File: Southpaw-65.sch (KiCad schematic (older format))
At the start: 205 parts, among them J1 USB_C_Receptacle_USB2.0, SW1 SW_Push, U1 ATmega32A-PU, Y1 16MHz

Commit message: More wiring
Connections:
- net COL0: now also U1.4 (PB3); no longer U1.35 (PA5)
- net COL1: now also U1.3 (PB2); no longer U1.34 (PA6)
- net COL10: no longer U1.8 (PB7)
- net COL11: no longer U1.22 (PC0)
- net COL12: no longer U1.23 (PC1)
- net COL13: no longer U1.24 (PC2)
- net COL14: no longer U1.25 (PC3)
- net COL15: no longer U1.26 (PC4)
- net COL16: no longer U1.27 (PC5)
- net COL17: no longer U1.28 (PC6)
- net COL18: no longer U1.29 (PC7)
- net COL19: no longer U1.14 (PD0)
- net COL2: now also U1.2 (PB1); no longer U1.33 (PA7)
- net COL4: now also U1.39 (PA1); no longer U1.2 (PB1)
- net COL5: now also U1.40 (PA0); no longer U1.3 (PB2)
- net COL6: no longer U1.4 (PB3)
- net COL7: no longer U1.5 (PB4)
- net COL8: no longer U1.6 (PB5)
- net COL9: no longer U1.7 (PB6)
- net ROW0: now also U1.5 (PB4); no longer U1.40 (PA0)
- net ROW1: now also U1.6 (PB5); no longer U1.39 (PA1)
- net ROW2: now also U1.7 (PB6); no longer U1.38 (PA2)
- net ROW3: now also U1.8 (PB7); no longer U1.37 (PA3)
- net ROW4: now also U1.14 (PD0); no longer U1.36 (PA4)
- no-connect marks 3 -> 0
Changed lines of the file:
@@
 Wire Wire Line
 	17400 3350 17400 4000
-Text GLabel 2000 1050 2    50   Input ~ 0
+Text GLabel 2000 2350 2    50   Input ~ 0
 ROW0
-Text GLabel 2000 1150 2    50   Input ~ 0
+Text GLabel 2000 2450 2    50   Input ~ 0
 ROW1
-Text GLabel 2000 1250 2    50   Input ~ 0
+Text GLabel 2000 2550 2    50   Input ~ 0
 ROW2
-Text GLabel 2000 1350 2    50   Input ~ 0
+Text GLabel 2000 2650 2    50   Input ~ 0
 ROW3
-Text GLabel 2000 1450 2    50   Input ~ 0
-ROW4
-Text GLabel 2000 1550 2    50   Input ~ 0
+Text GLabel 2000 2250 2    50   Input ~ 0
 COL0
-Text GLabel 2000 1650 2    50   Input ~ 0
+Text GLabel 2000 2150 2    50   Input ~ 0
 COL1
-Text GLabel 2000 1750 2    50   Input ~ 0
+Text GLabel 2000 2050 2    50   Input ~ 0
 COL2
 Text GLabel 2000 1950 2    50   Input ~ 0
 COL3
-Text GLabel 2000 2050 2    50   Input ~ 0
+Text GLabel 2000 1150 2    50   Input ~ 0
 COL4
-Text GLabel 2000 2150 2    50   Input ~ 0
+Text GLabel 2000 1050 2    50   Input ~ 0
 COL5
-Text GLabel 2000 2250 2    50   Input ~ 0
+Text GLabel 3050 2250 2    50   Input ~ 0
 COL6
-Text GLabel 2000 2350 2    50   Input ~ 0
+Text GLabel 3050 2350 2    50   Input ~ 0
 COL7
-Text GLabel 2000 2450 2    50   Input ~ 0
+Text GLabel 3050 2450 2    50   Input ~ 0
 COL8
-Text GLabel 2000 2550 2    50   Input ~ 0
+Text GLabel 3050 2550 2    50   Input ~ 0
 COL9
-Text GLabel 2000 2650 2    50   Input ~ 0
+Text GLabel 3050 2650 2    50   Input ~ 0
 COL10
-Text GLabel 2000 2850 2    50   Input ~ 0
+Text GLabel 3050 2850 2    50   Input ~ 0
 COL11
-Text GLabel 2000 2950 2    50   Input ~ 0
+Text GLabel 3050 2950 2    50   Input ~ 0
 COL12
-Text GLabel 2000 3050 2    50   Input ~ 0
+Text GLabel 3050 3050 2    50   Input ~ 0
 COL13
-Text GLabel 2000 3150 2    50   Input ~ 0
+Text GLabel 3050 3150 2    50   Input ~ 0
 COL14
-Text GLabel 2000 3250 2    50   Input ~ 0
+Text GLabel 3050 3250 2    50   Input ~ 0
 COL15
-Text GLabel 2000 3350 2    50   Input ~ 0
+Text GLabel 3050 3350 2    50   Input ~ 0
 COL16
-Text GLabel 2000 3450 2    50   Input ~ 0
+Text GLabel 3050 3450 2    50   Input ~ 0
 COL17
-Text GLabel 2000 3550 2    50   Input ~ 0
+Text GLabel 3050 3550 2    50   Input ~ 0
 COL18
-Text GLabel 2000 3750 2    50   Input ~ 0
+Text GLabel 3050 3750 2    50   Input ~ 0
 COL19
 $Comp
@@
 Wire Wire Line
 	1400 750  1400 700
-Connection ~ 1400 750
 $Comp
 L power:GND #PWR0110
@@
 Wire Wire Line
 	2800 4050 2700 4050
-$Comp
-L MCU_Microchip_ATmega:ATmega32A-PU U1
-U 1 1 5F901AE8
-P 1400 2750
-F 0 "U1" H 1400 661 50  0000 C CNN
-F 1 "ATmega32A-PU" H 1400 570 50  0000 C CNN
-F 2 "Package_DIP:DIP-40_W15.24mm" H 1400 2750 50  0001 C CIN
-F 3 "http://ww1.microchip.com/downloads/en/DeviceDoc/atmel-8155-8-bit-microcontroller-avr-atmega32a_datasheet.pdf" H 1400 2750 50  0001 C CNN
-	1    1400 2750
-	1    0    0    -1
-$EndComp
-NoConn ~ 2000 4450
-NoConn ~ 2000 4350
-NoConn ~ 2000 3850
 Wire Wire Line
 	14950 2050 14950 2700
@@
 Wire Wire Line
 	16200 1250 16200 1400
+Text GLabel 2000 3750 2    50   Input ~ 0
+ROW4
+Connection ~ 1400 750
+$Comp
+L MCU_Microchip_ATmega:ATmega32A-PU U1
+U 1 1 5F901AE8
+P 1400 2750
+F 0 "U1" H 1400 661 50  0000 C CNN
+F 1 "ATmega32A-PU" H 1400 570 50  0000 C CNN
+F 2 "Package_DIP:DIP-40_W15.24mm" H 1400 2750 50  0001 C CIN
+F 3 "http://ww1.microchip.com/downloads/en/DeviceDoc/atmel-8155-8-bit-microcontroller-avr-atmega32a_datasheet.pdf" H 1400 2750 50  0001 C CNN
+	1    1400 2750
+	1    0    0    -1
+$EndComp
 $EndSCHEMATC

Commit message: Lots of wiring to MCU done
Considering redoing it because thicc bottom
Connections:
- net COL10: now also U1.34 (PA6)
- net COL11: now also U1.35 (PA5)
- net COL12: now also U1.36 (PA4)
- net COL13: now also U1.37 (PA3)
- net COL14: now also U1.38 (PA2)
- net COL15: now also U1.24 (PC2)
- net COL16: now also U1.25 (PC3)
- net COL17: now also U1.27 (PC5)
- net COL18: now also U1.15 (PD1)
- net COL19: now also U1.20 (PD6)
- net COL7: now also U1.29 (PC7)
- net COL8: now also U1.32 (AREF)
- net COL9: now also U1.33 (PA7)
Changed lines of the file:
@@
 Text GLabel 2000 1050 2    50   Input ~ 0
 COL5
-Text GLabel 3050 2250 2    50   Input ~ 0
-COL6
-Text GLabel 3050 2350 2    50   Input ~ 0
-COL7
-Text GLabel 3050 2450 2    50   Input ~ 0
+Text GLabel 800  1650 0    50   Input ~ 0
 COL8
-Text GLabel 3050 2550 2    50   Input ~ 0
+Text GLabel 2000 1750 2    50   Input ~ 0
 COL9
-Text GLabel 3050 2650 2    50   Input ~ 0
+Text GLabel 2000 1650 2    50   Input ~ 0
 COL10
-Text GLabel 3050 2850 2    50   Input ~ 0
+Text GLabel 2000 1550 2    50   Input ~ 0
 COL11
-Text GLabel 3050 2950 2    50   Input ~ 0
+Text GLabel 2000 1450 2    50   Input ~ 0
 COL12
-Text GLabel 3050 3050 2    50   Input ~ 0
+Text GLabel 2000 1350 2    50   Input ~ 0
 COL13
-Text GLabel 3050 3150 2    50   Input ~ 0
+Text GLabel 2000 1250 2    50   Input ~ 0
 COL14
-Text GLabel 3050 3250 2    50   Input ~ 0
+Text GLabel 2000 3050 2    50   Input ~ 0
 COL15
-Text GLabel 3050 3350 2    50   Input ~ 0
+Text GLabel 2000 3150 2    50   Input ~ 0
 COL16
-Text GLabel 3050 3450 2    50   Input ~ 0
+Text GLabel 2000 3350 2    50   Input ~ 0
 COL17
-Text GLabel 3050 3550 2    50   Input ~ 0
+Text GLabel 2000 3850 2    50   Input ~ 0
 COL18
-Text GLabel 3050 3750 2    50   Input ~ 0
+Text GLabel 2000 4350 2    50   Input ~ 0
 COL19
 $Comp
@@
 	1    0    0    -1
 $EndComp
+Text GLabel 2000 3550 2    50   Input ~ 0
+COL7
+Text GLabel 3050 2250 2    50   Input ~ 0
+COL6
 $EndSCHEMATC

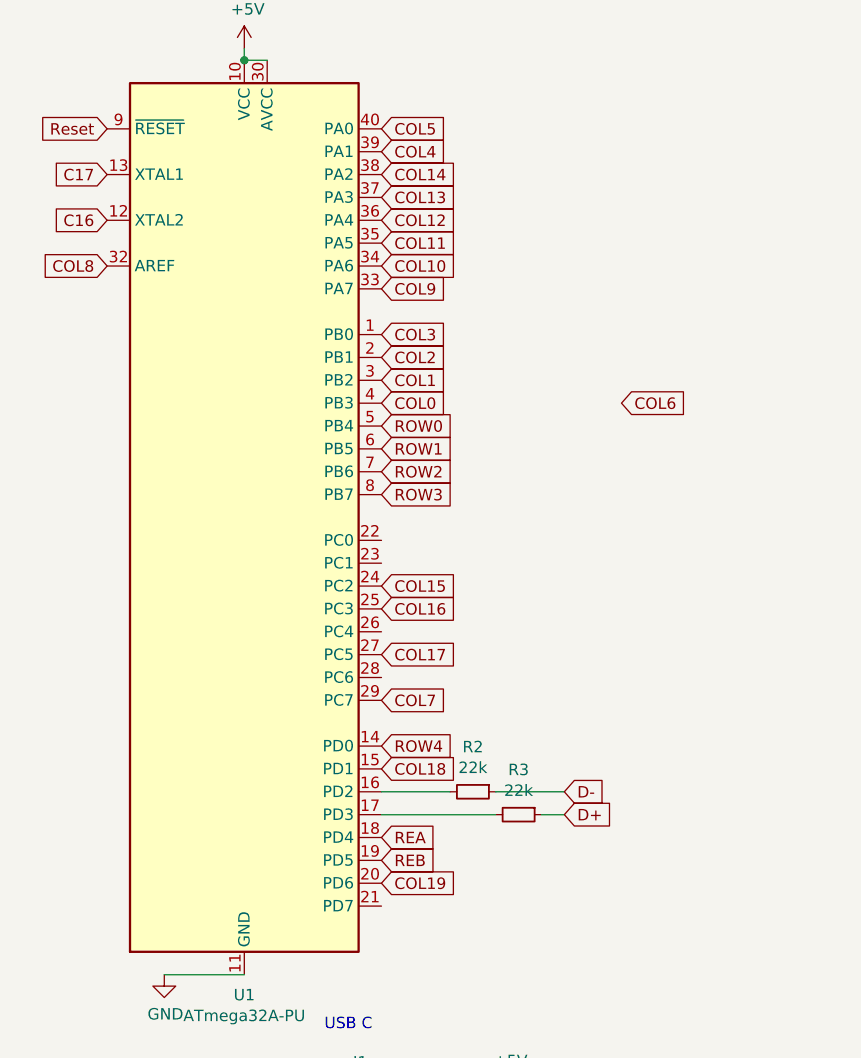
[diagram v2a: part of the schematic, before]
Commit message: Redid wirings
Decrease in space between pcb bottom, and switches
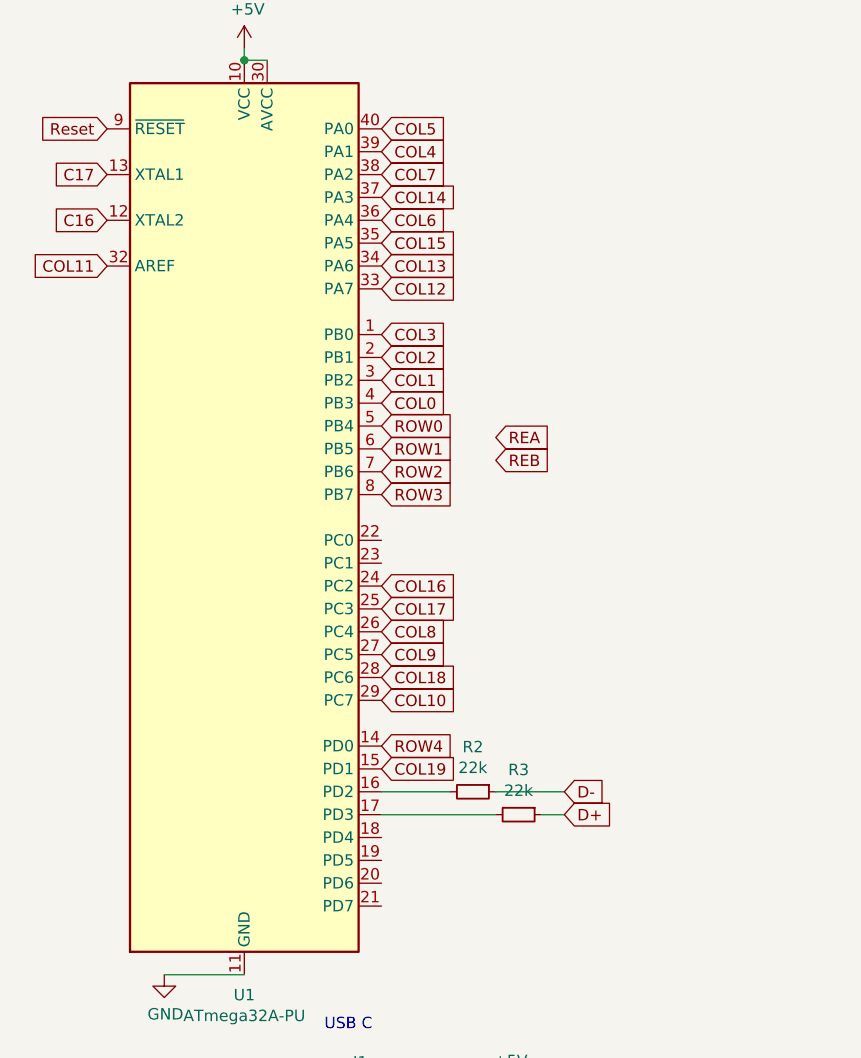
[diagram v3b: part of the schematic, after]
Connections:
- net COL10: now also U1.29 (PC7); no longer U1.34 (PA6)
- net COL11: now also U1.32 (AREF); no longer U1.35 (PA5)
- net COL12: now also U1.33 (PA7); no longer U1.36 (PA4)
- net COL13: now also U1.34 (PA6); no longer U1.37 (PA3)
- net COL14: now also U1.37 (PA3); no longer U1.38 (PA2)
- net COL15: now also U1.35 (PA5); no longer U1.24 (PC2)
- net COL16: now also U1.24 (PC2); no longer U1.25 (PC3)
- net COL17: now also U1.25 (PC3); no longer U1.27 (PC5)
- net COL18: now also U1.28 (PC6); no longer U1.15 (PD1)
- net COL19: now also U1.15 (PD1); no longer U1.20 (PD6)
- net COL6: now also U1.36 (PA4)
- net COL7: now also U1.38 (PA2); no longer U1.29 (PC7)
- net COL8: now also U1.26 (PC4); no longer U1.32 (AREF)
- net COL9: now also U1.27 (PC5); no longer U1.33 (PA7)
- net REA: no longer U1.18 (PD4)
- net REB: no longer U1.19 (PD5)
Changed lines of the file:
@@
 Text GLabel 2000 1050 2    50   Input ~ 0
 COL5
+Text GLabel 2000 3250 2    50   Input ~ 0
+COL8
+Text GLabel 2000 3350 2    50   Input ~ 0
+COL9
+Text GLabel 2000 3550 2    50   Input ~ 0
+COL10
 Text GLabel 800  1650 0    50   Input ~ 0
-COL8
+COL11
 Text GLabel 2000 1750 2    50   Input ~ 0
-COL9
+COL12
 Text GLabel 2000 1650 2    50   Input ~ 0
-COL10
+COL13
+Text GLabel 2000 1350 2    50   Input ~ 0
+COL14
 Text GLabel 2000 1550 2    50   Input ~ 0
-COL11
-Text GLabel 2000 1450 2    50   Input ~ 0
-COL12
-Text GLabel 2000 1350 2    50   Input ~ 0
-COL13
-Text GLabel 2000 1250 2    50   Input ~ 0
-COL14
+COL15
 Text GLabel 2000 3050 2    50   Input ~ 0
-COL15
+COL16
 Text GLabel 2000 3150 2    50   Input ~ 0
-COL16
-Text GLabel 2000 3350 2    50   Input ~ 0
 COL17
+Text GLabel 2000 3450 2    50   Input ~ 0
+COL18
 Text GLabel 2000 3850 2    50   Input ~ 0
-COL18
-Text GLabel 2000 4350 2    50   Input ~ 0
 COL19
 $Comp
@@
 Text Notes 5250 5000 0    50   ~ 0
 Reset
-Text GLabel 2000 4150 2    50   Input ~ 0
+Text GLabel 2500 2400 2    50   Input ~ 0
 REA
-Text GLabel 2000 4250 2    50   Input ~ 0
+Text GLabel 2500 2500 2    50   Input ~ 0
 REB
 Wire Wire Line
@@
 	1    0    0    -1
 $EndComp
-Text GLabel 2000 3550 2    50   Input ~ 0
+Text GLabel 2000 1250 2    50   Input ~ 0
 COL7
-Text GLabel 3050 2250 2    50   Input ~ 0
+Text GLabel 2000 1450 2    50   Input ~ 0
 COL6
 $EndSCHEMATC

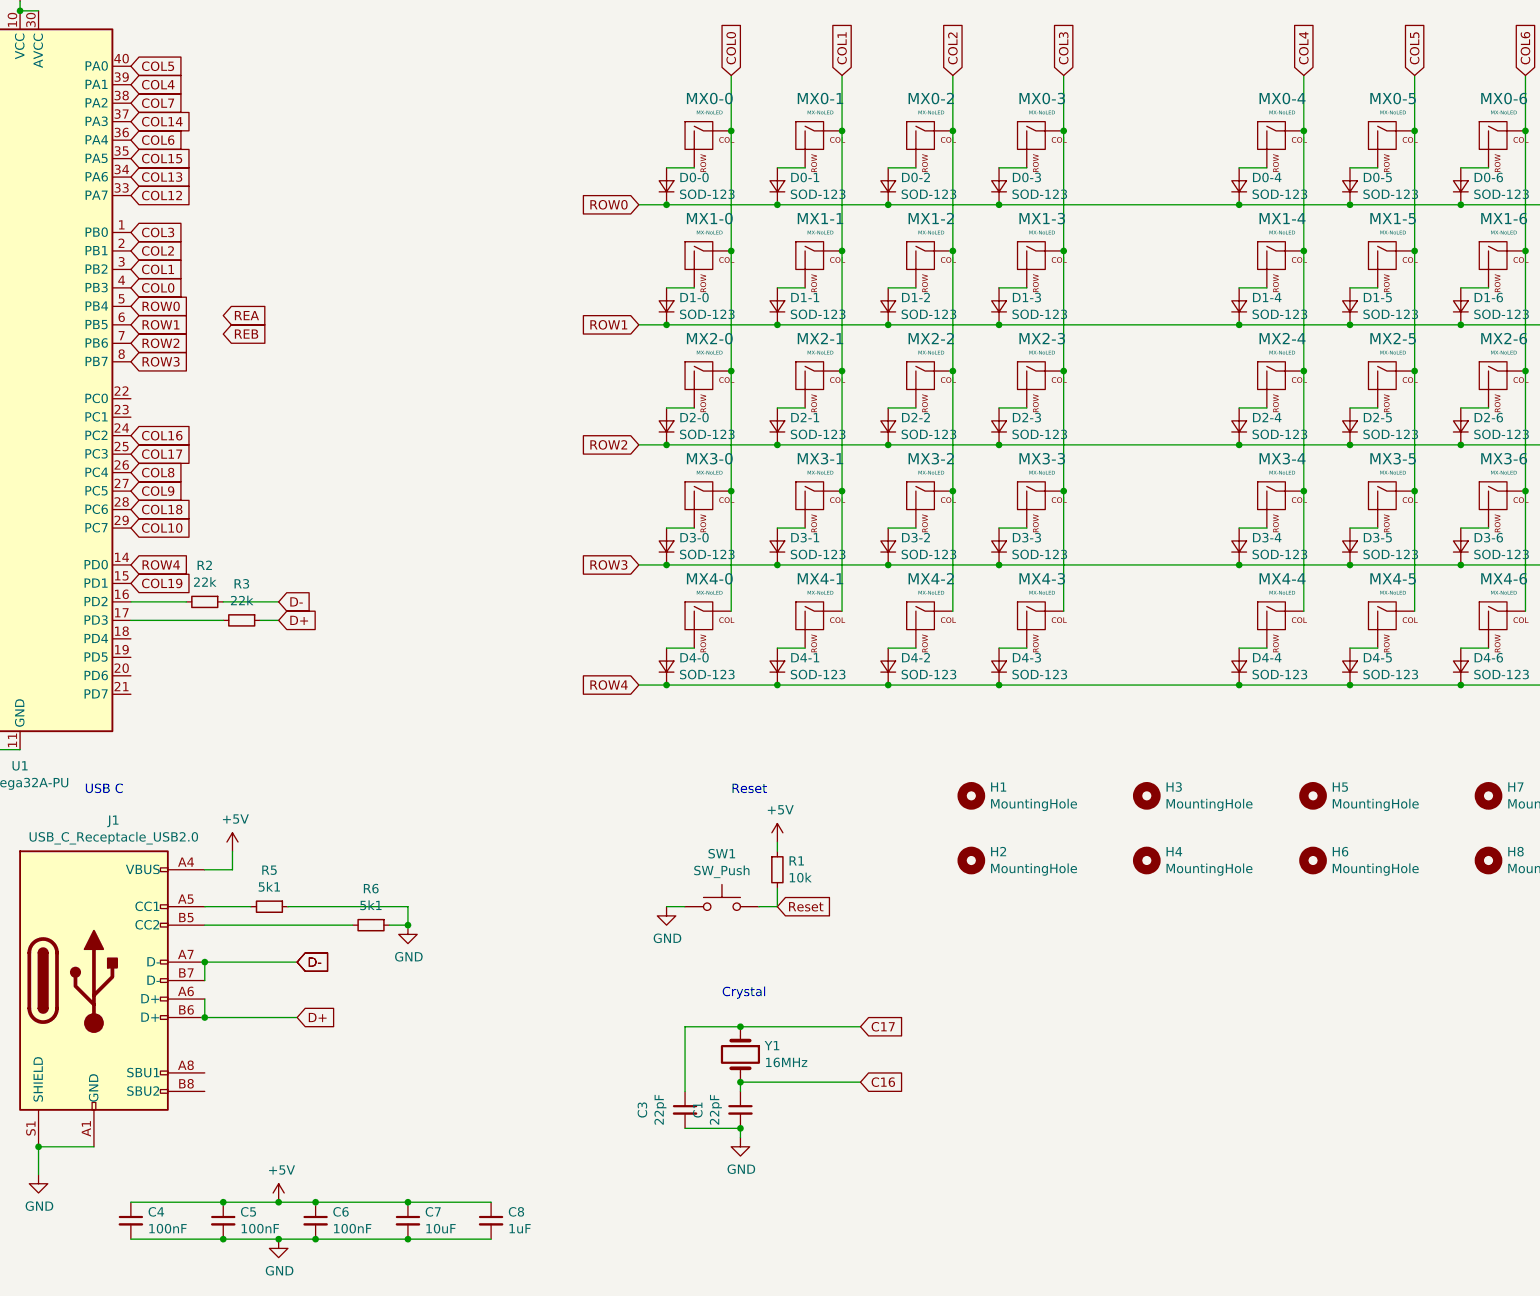
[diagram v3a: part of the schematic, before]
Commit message: Added encoders
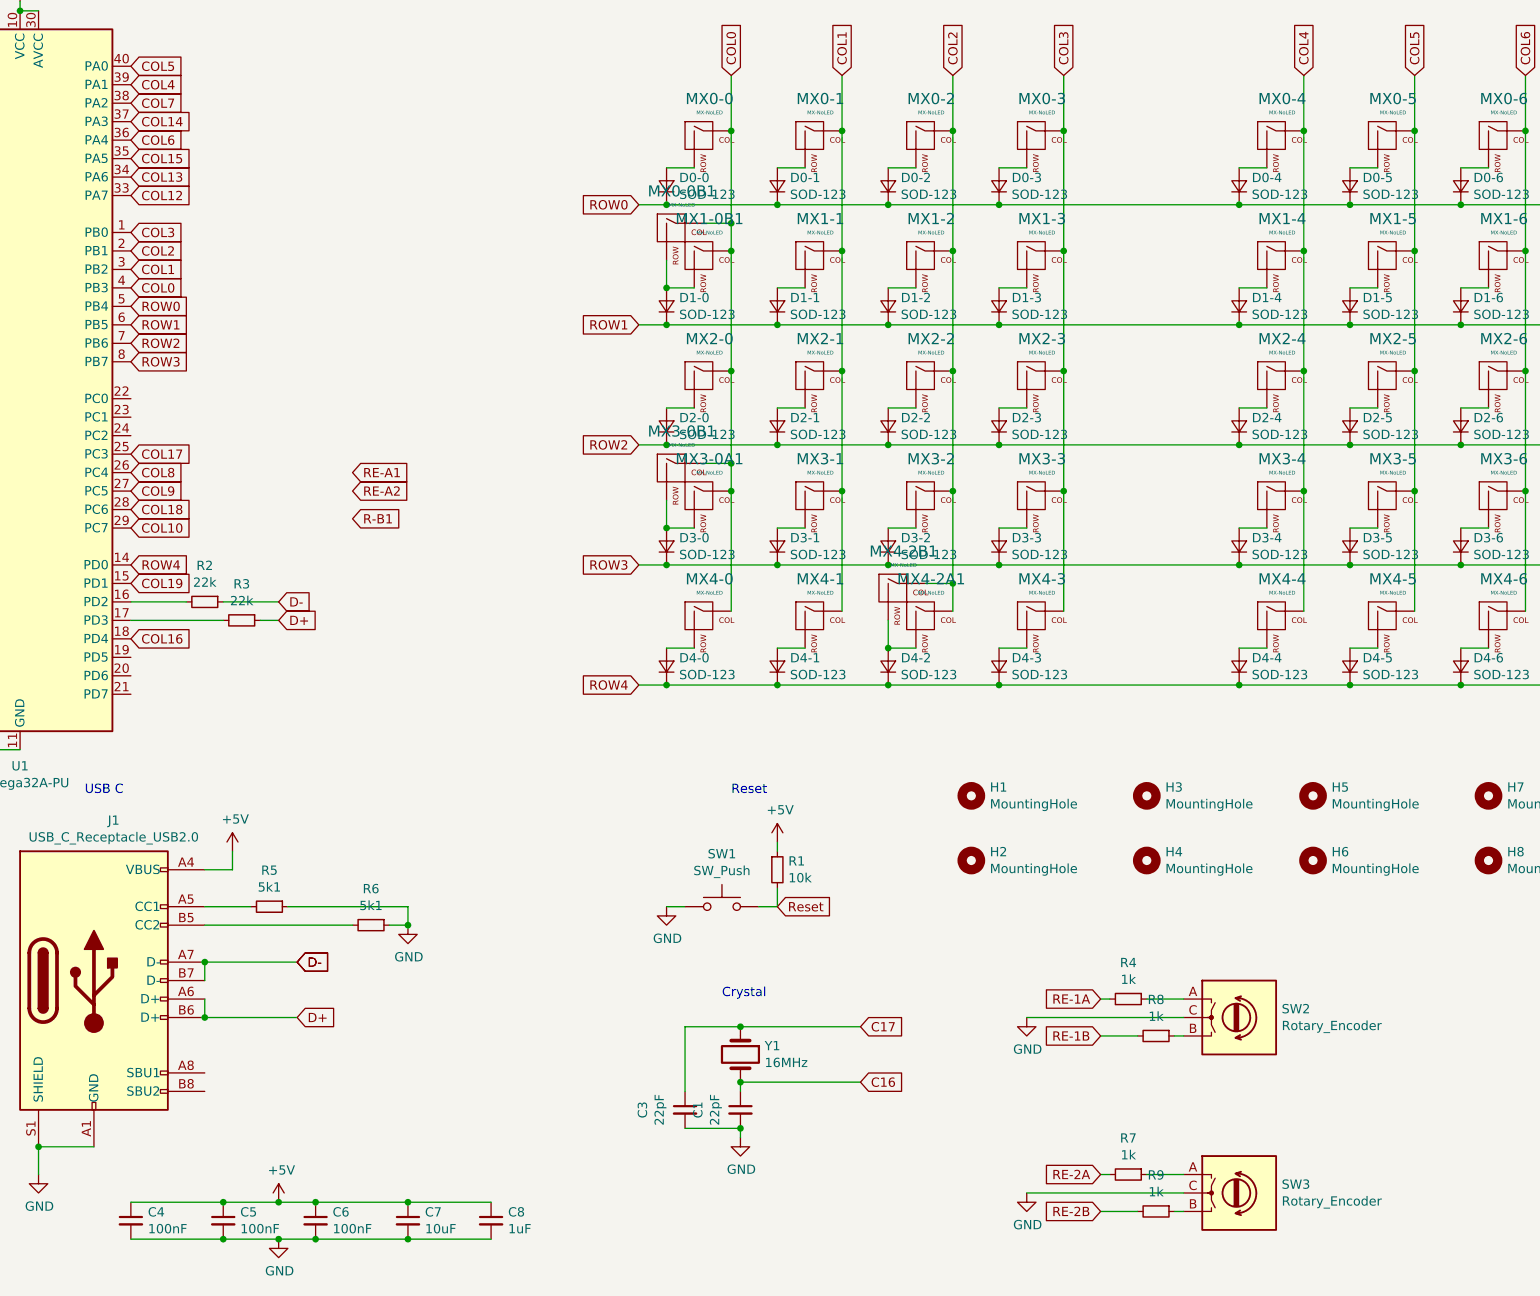
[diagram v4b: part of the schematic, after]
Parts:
- added MX0-0B1, MX3-0B1, MX4-2B1: MX-NoLED, MX_Only:MXOnly-2U, symbol MX_Alps_Hybrid:MX-NoLED
- added R4, R7, R8, R9: 1k, Resistor_THT:R_Axial_DIN0207_L6.3mm_D2.5mm_P7.62mm_Horizontal, symbol Device:R_Small
- added SW2, SW3: Rotary_Encoder, Rotary_Encoder:RotaryEncoder_Alps_EC11E_Vertical_H20mm, symbol Device:Rotary_Encoder
- MX0-0, MX0-1, MX0-10, MX0-11, MX0-12, MX0-13, MX0-14, MX0-15, MX0-16, MX0-17A1, MX0-18, MX0-19, MX0-2, MX0-3, MX0-4, MX0-5, MX0-6, MX0-7, MX0-8, MX0-9, MX1-1, MX1-10, MX1-11, MX1-12, MX1-13, MX1-14, MX1-15, MX1-16, MX1-19, MX1-2, MX1-3, MX1-5, MX1-6, MX1-7, MX1-8, MX1-9, MX2-0, MX2-1, MX2-10, MX2-11, MX2-12, MX2-13, MX2-14, MX2-15, MX2-19, MX2-2, MX2-3, MX2-5, MX2-6, MX2-7, MX2-8, MX2-9, MX3-1, MX3-10, MX3-11, MX3-12, MX3-13, MX3-14, MX3-18, MX3-19, MX3-2, MX3-3, MX3-5, MX3-6, MX3-7, MX3-8, MX3-9, MX4-0, MX4-1, MX4-14, MX4-15, MX4-18, MX4-19, MX4-3, MX4-5: footprint MX_Alps_Hybrid:MX-1U -> MX_Only:MXOnly-1U
- MX0-17B1: footprint MX_Alps_Hybrid:MX-2U -> MX_Only:MXOnly-2U
- MX1-0B1: renamed from MX1-0; footprint MX_Alps_Hybrid:MX-1U -> MX_Only:MXOnly-1U
- MX1-18, MX1-4, MX4-4: footprint MX_Alps_Hybrid:MX-1.5U -> MX_Only:MXOnly-1.5U
- MX2-18, MX3-4: footprint MX_Alps_Hybrid:MX-2.25U -> MX_Only:MXOnly-2.25U
- MX2-4, MX3-15: footprint MX_Alps_Hybrid:MX-1.75U -> MX_Only:MXOnly-1.75U
- MX3-0A1: renamed from MX3-0; footprint MX_Alps_Hybrid:MX-1U -> MX_Only:MXOnly-1U
- MX4-10: footprint MX_Alps_Hybrid:MX-7U -> MX_Only:MXOnly-7U
- MX4-12, MX4-8: footprint MX_Alps_Hybrid:MX-3U -> MX_Only:MXOnly-3U
- MX4-13, MX4-6: footprint MX_Alps_Hybrid:MX-1.25U -> MX_Only:MXOnly-1.25U
- MX4-2A1: renamed from MX4-2; footprint MX_Alps_Hybrid:MX-1U -> MX_Only:MXOnly-1U
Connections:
- net COL0: now also MX0-0B1.1 (COL), MX3-0B1.1 (COL)
- net COL16: now also U1.18 (PD4); no longer U1.24 (PC2)
- net COL2: now also MX4-2B1.1 (COL)
- net GND: now also SW2.C, SW3.C
- net at D1-0.2 (A), MX1-0B1.2 (ROW): now also MX0-0B1.2 (ROW)
- net at D3-0.2 (A), MX3-0A1.2 (ROW): now also MX3-0B1.2 (ROW)
- net at D4-2.2 (A), MX4-2A1.2 (ROW): now also MX4-2B1.2 (ROW)
- new net: R4.1, SW2.A
- new net: R8.1, SW2.B
- new net: R7.1, SW3.A
- new net: R9.1, SW3.B
- new net RE-1A: R4.2
- new net RE-1B: R8.2
- new net RE-2A: R7.2
- new net RE-2B: R9.2
